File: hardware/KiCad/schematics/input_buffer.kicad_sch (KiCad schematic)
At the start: 11 parts, among them U1 MCP6022

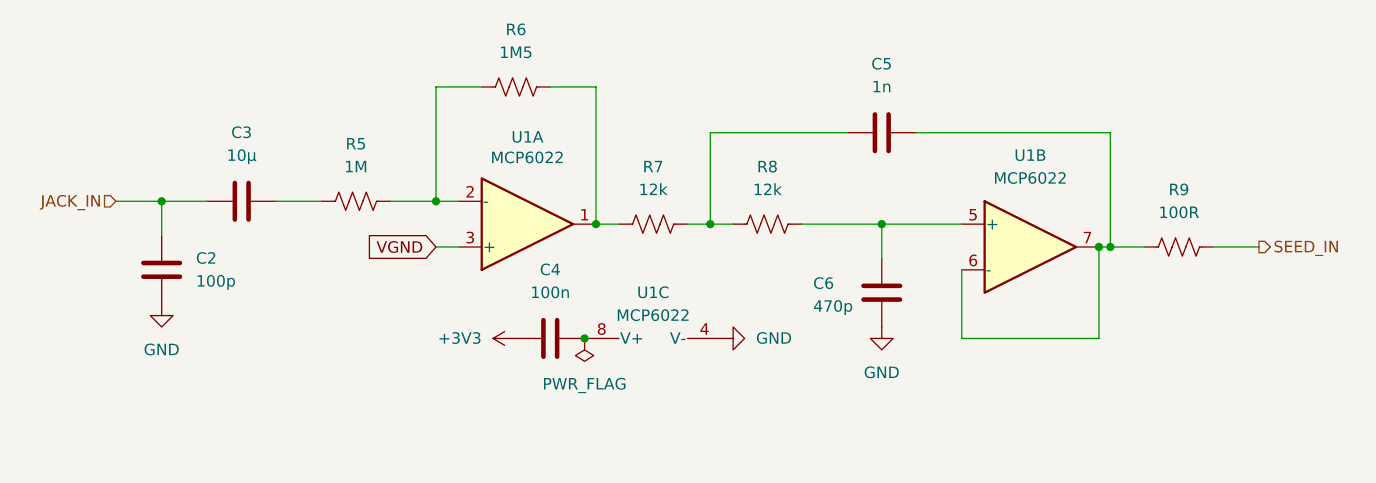
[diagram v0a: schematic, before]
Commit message: Adding op amps to board; bypass cap correction.
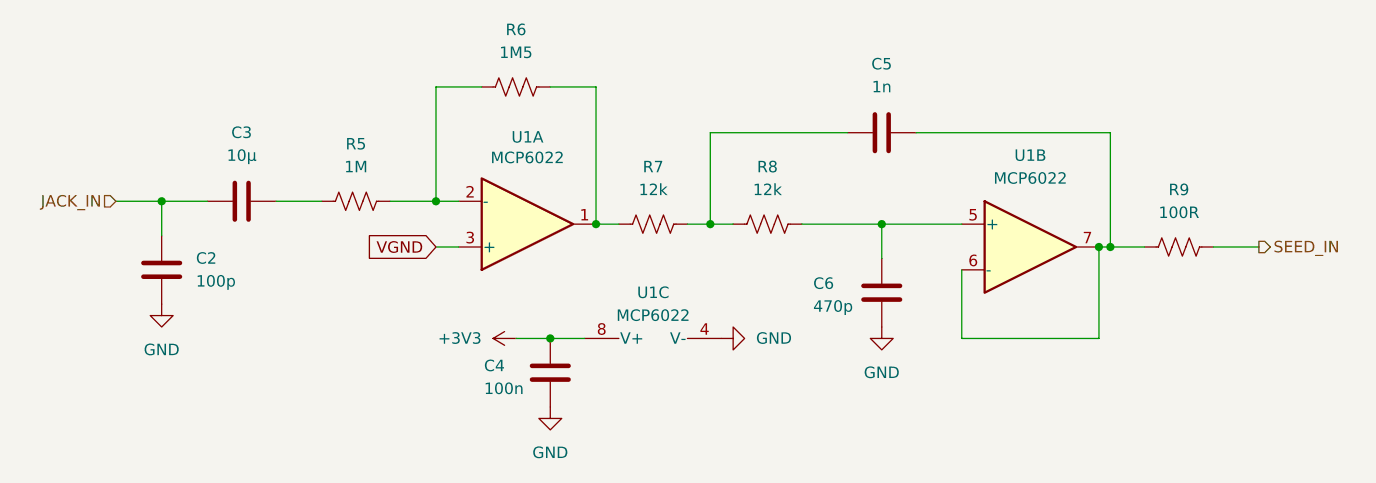
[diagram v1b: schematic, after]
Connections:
- net +3V3: now also U1.8 (V+)
- net GND: now also C4.2
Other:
- moved on the sheet: C4
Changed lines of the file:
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@@
-	)
-	(junction
-		(at 137.16 115.57)
-		(diameter 0)
-		(color 0 0 0 0)
 	)
 	(junction
@@
 		(color 0 0 0 0)
 	)
+	(junction
+		(at 133.35 115.57)
+		(diameter 0)
+		(color 0 0 0 0)
+	)
 	(wire
 		(pts
@@
 		(pts
 			(xy 133.35 87.63) (xy 138.43 87.63)
+		)
+		(stroke
+			(width 0)
+			(type default)
+		)
+	)
+	(wire
+		(pts
+			(xy 129.54 115.57) (xy 133.35 115.57)
+		)
+		(stroke
+			(width 0)
+			(type default)
+		)
+	)
+	(wire
+		(pts
+			(xy 133.35 115.57) (xy 137.16 115.57)
 		)
 		(stroke
@@
 	(symbol
 		(lib_id "power:GND")
+		(at 133.35 123.19 0)
+		(unit 1)
+		(body_style 1)
+		(exclude_from_sim no)
+		(in_bom yes)
+		(on_board yes)
+		(in_pos_files yes)
+		(dnp no)
+		(fields_autoplaced yes)
+		(property "Reference" "#PWR029"
+			(at 133.35 129.54 0)
+			(hide yes)
+			(show_name no)
+			(do_not_autoplace no)
+			(effects
+				(font
+					(size 1.27 1.27)
+				)
+			)
+		)
+		(property "Value" "GND"
+			(at 133.35 128.27 0)
+			(show_name no)
+			(do_not_autoplace no)
+			(effects
+				(font
+					(size 1.27 1.27)
+				)
+			)
+		)
+		(property "Footprint" ""
+			(at 133.35 123.19 0)
+			(hide yes)
+			(show_name no)
+			(do_not_autoplace no)
+			(effects
+				(font
+					(size 1.27 1.27)
+				)
+			)
+		)
+		(property "Datasheet" ""
+			(at 133.35 123.19 0)
+			(hide yes)
+			(show_name no)
+			(do_not_autoplace no)
+			(effects
+				(font
+					(size 1.27 1.27)
+				)
+			)
+		)
+		(property "Description" "Power symbol creates a global label with name \"GND\" , ground"
+			(at 133.35 123.19 0)
+			(hide yes)
+			(show_name no)
+			(do_not_autoplace no)
+			(effects
+				(font
+					(size 1.27 1.27)
+				)
+			)
+		)
+		(pin "1"
+		)
+		(instances
+			(project "mimeofreq"
+				(path "/fc444d3c-3a1a-4715-bcff-119f4d2b4d9e/5a5a17f9-5733-4e29-97e0-85beffe17bcf"
+					(reference "#PWR029")
+					(unit 1)
+				)
+			)
+		)
+	)
+	(symbol
+		(lib_id "power:GND")
 		(at 152.4 115.57 90)
 		(unit 1)
@@
 	(symbol
 		(lib_id "Device:C")
-		(at 133.35 115.57 90)
+		(at 133.35 119.38 0)
 		(unit 1)
 		(body_style 1)
@@
 		(in_pos_files yes)
 		(dnp no)
-		(fields_autoplaced yes)
 		(property "Reference" "C4"
-			(at 133.35 107.95 90)
-			(show_name no)
-			(do_not_autoplace no)
-			(effects
-				(font
-					(size 1.27 1.27)
-				)
+			(at 125.984 118.618 0)
+			(show_name no)
+			(do_not_autoplace no)
+			(effects
+				(font
+					(size 1.27 1.27)
+				)
+				(justify left)
 			)
 		)
 		(property "Value" "100n"
-			(at 133.35 110.49 90)
-			(show_name no)
-			(do_not_autoplace no)
-			(effects
-				(font
-					(size 1.27 1.27)
-				)
+			(at 125.984 121.158 0)
+			(show_name no)
+			(do_not_autoplace no)
+			(effects
+				(font
+					(size 1.27 1.27)
+				)
+				(justify left)
 			)
 		)
 		(property "Footprint" "Capacitor_THT_Custom:C_Rect_L4.0mm_W2.6mm_P2.50mm"
-			(at 137.16 114.6048 0)
+			(at 134.3152 123.19 0)
 			(hide yes)
 			(show_name no)
@@
 		)
 		(property "Datasheet" ""
-			(at 133.35 115.57 0)
+			(at 133.35 119.38 0)
 			(hide yes)
 			(show_name no)
@@
 		)
 		(property "Description" "Unpolarized capacitor"
-			(at 133.35 115.57 0)
+			(at 133.35 119.38 0)
 			(hide yes)
 			(show_name no)
@@
 					(unit 1)
 				)
-			)
-		)
-	)
-	(symbol
-		(lib_id "power:PWR_FLAG")
-		(at 137.16 115.57 180)
-		(unit 1)
-		(body_style 1)
-		(exclude_from_sim no)
-		(in_bom yes)
-		(on_board yes)
-		(in_pos_files yes)
-		(dnp no)
-		(fields_autoplaced yes)
-		(property "Reference" "#FLG04"
-			(at 137.16 117.475 0)
-			(hide yes)
-			(show_name no)
-			(do_not_autoplace no)
-			(effects
-				(font
-					(size 1.27 1.27)
-				)
-			)
-		)
-		(property "Value" "PWR_FLAG"
-			(at 137.16 120.65 0)
-			(show_name no)
-			(do_not_autoplace no)
-			(effects
-				(font
-					(size 1.27 1.27)
-				)
-			)
-		)
-		(property "Footprint" ""
-			(at 137.16 115.57 0)
-			(hide yes)
-			(show_name no)
-			(do_not_autoplace no)
-			(effects
-				(font
-					(size 1.27 1.27)
-				)
-			)
-		)
-		(property "Datasheet" ""
-			(at 137.16 115.57 0)
-			(hide yes)
-			(show_name no)
-			(do_not_autoplace no)
-			(effects
-				(font
-					(size 1.27 1.27)
-				)
-			)
-		)
-		(property "Description" "Special symbol for telling ERC where power comes from"
-			(at 137.16 115.57 0)
-			(hide yes)
-			(show_name no)
-			(do_not_autoplace no)
-			(effects
-				(font
-					(size 1.27 1.27)
-				)
-			)
-		)
-		(pin "1"
-		)
-		(instances
-			(project "mimeofreq"
-				(path "/fc444d3c-3a1a-4715-bcff-119f4d2b4d9e/5a5a17f9-5733-4e29-97e0-85beffe17bcf"
-					(reference "#FLG04")
-					(unit 1)
-				)

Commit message: All components fit on PCB. Some footprints replaced.
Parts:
- C3: footprint Capacitor_THT:C_Rect_L7.0mm_W2.5mm_P5.00mm -> Capacitor_THT:C_Rect_L4.0mm_W2.5mm_P2.50mm
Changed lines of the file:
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@@
 			)
 		)
-		(property "Footprint" "Capacitor_THT:C_Rect_L7.0mm_W2.5mm_P5.00mm"
+		(property "Footprint" "Capacitor_THT:C_Rect_L4.0mm_W2.5mm_P2.50mm"
 			(at 95.25 101.2952 0)
 			(hide yes)
